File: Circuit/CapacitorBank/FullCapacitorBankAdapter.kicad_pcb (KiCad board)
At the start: 2 copper layers, 116.8 x 61 mm, 46 parts, among them J1 AC Power In, J2 Output+, J3 Output-, J4 To Control, T1 6:6:50+50, U1 L7812, U2 LM393, U3 LM393, U4 PC817

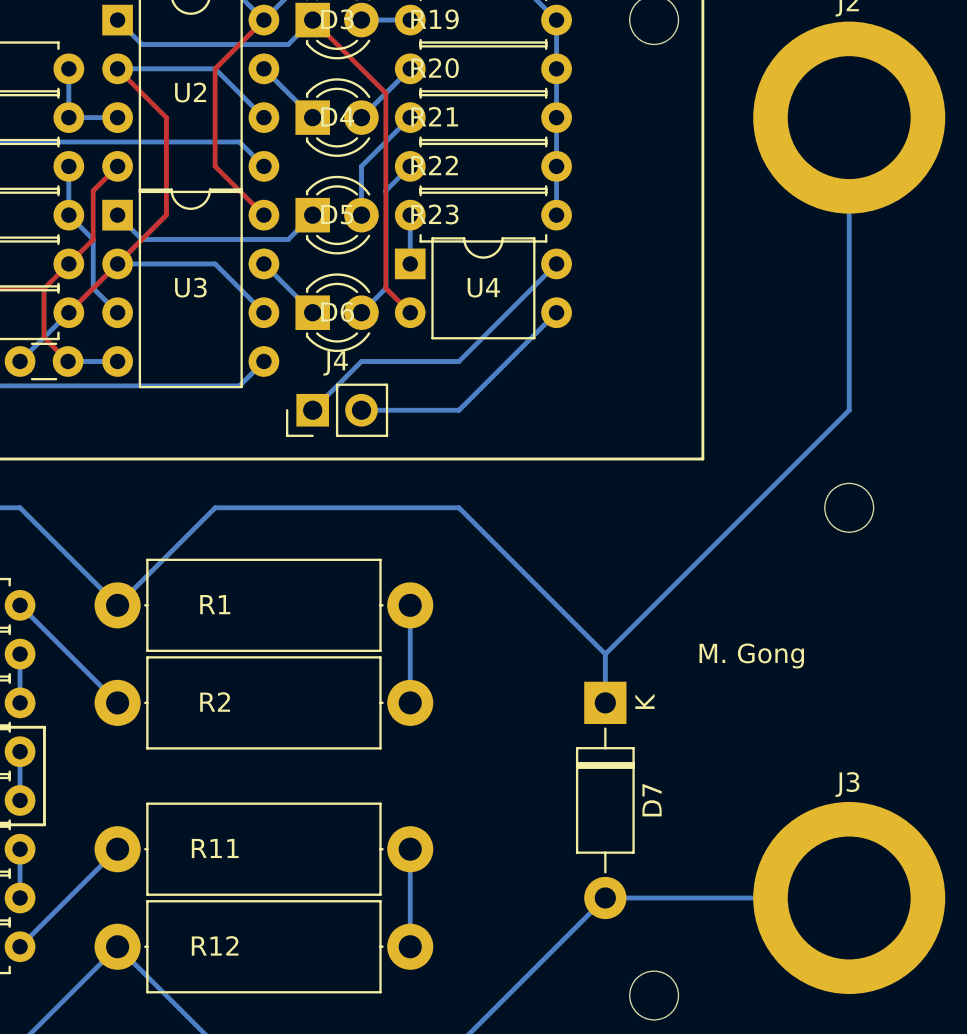
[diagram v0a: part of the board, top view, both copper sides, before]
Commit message: [Circuit][Doc] Correct the voltage calculation in full capacitor bank adapter
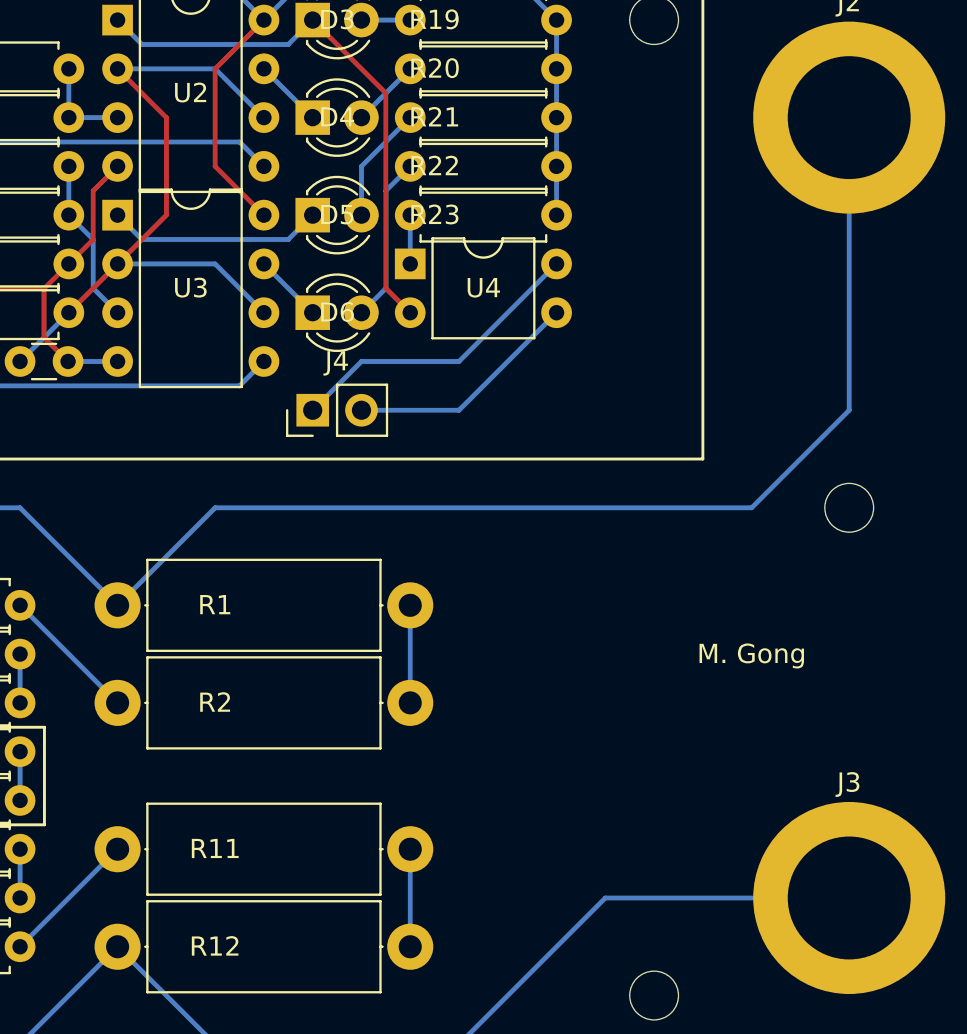
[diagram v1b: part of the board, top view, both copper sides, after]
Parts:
- removed D7: 1N4007, Diode_THT:D_DO-41_SOD81_P10.16mm_Horizontal
- T1: value 6:6:50+50 -> 6:6:33+33
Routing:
- net /PowerOut+: track 110.4 -> 101.5 mm
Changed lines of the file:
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@@
     (thickness 1.6)
     (drawings 17)
-    (tracks 161)
+    (tracks 159)
     (zones 0)
-    (modules 46)
+    (modules 45)
     (nets 40)
   )
@@
     )
   )
-  (module Diode_THT:D_DO-41_SOD81_P10.16mm_Horizontal (layer F.Cu)
-    (at 144.78 71.12 270)
-    (descr "Diode, DO-41_SOD81 series, Axial, Horizontal, pin pitch=10.16mm, , length*diameter=5.2*2.7mm^2, , http://www.diodes.com/_files/packages/DO-41%20(Plastic).pdf")
-    (tags "Diode DO-41_SOD81 series Axial Horizontal pin pitch 10.16mm  length 5.2mm diameter 2.7mm")
-    (fp_text reference D7 (at 5.08 -2.47 90) (layer F.SilkS)
-      (effects (font (size 1 1) (thickness 0.15)))
-    )
-    (fp_text value 1N4007 (at 5.08 2.47 90) (layer F.Fab)
-      (effects (font (size 1 1) (thickness 0.15)))
-    )
-    (fp_text user K (at 0 -2.1 90) (layer F.SilkS)
-      (effects (font (size 1 1) (thickness 0.15)))
-    )
-    (fp_text user K (at 0 -2.1 90) (layer F.Fab)
-      (effects (font (size 1 1) (thickness 0.15)))
-    )
-    (fp_text user %R (at 5.47 0 90) (layer F.Fab)
-      (effects (font (size 1 1) (thickness 0.15)))
-    )
-    (fp_line (start 11.51 -1.6) (end -1.35 -1.6) (layer F.CrtYd) (width 0.05))
-    (fp_line (start 11.51 1.6) (end 11.51 -1.6) (layer F.CrtYd) (width 0.05))
-    (fp_line (start -1.35 1.6) (end 11.51 1.6) (layer F.CrtYd) (width 0.05))
-    (fp_line (start -1.35 -1.6) (end -1.35 1.6) (layer F.CrtYd) (width 0.05))
-    (fp_line (start 3.14 -1.47) (end 3.14 1.47) (layer F.SilkS) (width 0.12))
-    (fp_line (start 3.38 -1.47) (end 3.38 1.47) (layer F.SilkS) (width 0.12))
-    (fp_line (start 3.26 -1.47) (end 3.26 1.47) (layer F.SilkS) (width 0.12))
-    (fp_line (start 8.82 0) (end 7.8 0) (layer F.SilkS) (width 0.12))
-    (fp_line (start 1.34 0) (end 2.36 0) (layer F.SilkS) (width 0.12))
-    (fp_line (start 7.8 -1.47) (end 2.36 -1.47) (layer F.SilkS) (width 0.12))
-    (fp_line (start 7.8 1.47) (end 7.8 -1.47) (layer F.SilkS) (width 0.12))
-    (fp_line (start 2.36 1.47) (end 7.8 1.47) (layer F.SilkS) (width 0.12))
-    (fp_line (start 2.36 -1.47) (end 2.36 1.47) (layer F.SilkS) (width 0.12))
-    (fp_line (start 3.16 -1.35) (end 3.16 1.35) (layer F.Fab) (width 0.1))
-    (fp_line (start 3.36 -1.35) (end 3.36 1.35) (layer F.Fab) (width 0.1))
-    (fp_line (start 3.26 -1.35) (end 3.26 1.35) (layer F.Fab) (width 0.1))
-    (fp_line (start 10.16 0) (end 7.68 0) (layer F.Fab) (width 0.1))
-    (fp_line (start 0 0) (end 2.48 0) (layer F.Fab) (width 0.1))
-    (fp_line (start 7.68 -1.35) (end 2.48 -1.35) (layer F.Fab) (width 0.1))
-    (fp_line (start 7.68 1.35) (end 7.68 -1.35) (layer F.Fab) (width 0.1))
-    (fp_line (start 2.48 1.35) (end 7.68 1.35) (layer F.Fab) (width 0.1))
-    (fp_line (start 2.48 -1.35) (end 2.48 1.35) (layer F.Fab) (width 0.1))
-    (pad 2 thru_hole oval (at 10.16 0 270) (size 2.2 2.2) (drill 1.1) (layers *.Cu *.Mask)
-      (net 2 /PowerOut-))
-    (pad 1 thru_hole rect (at 0 0 270) (size 2.2 2.2) (drill 1.1) (layers *.Cu *.Mask)
-      (net 1 /PowerOut+))
-    (model ${KISYS3DMOD}/Diode_THT.3dshapes/D_DO-41_SOD81_P10.16mm_Horizontal.wrl
-      (at (xyz 0 0 0))
-      (scale (xyz 1 1 1))
-      (rotate (xyz 0 0 0))
-    )
-  )
   (module Power:Heatsink_TO220_15x10mm (layer F.Cu)
     (at 78.74 34.29)
@@
       (effects (font (size 1 1) (thickness 0.15)))
     )
-    (fp_text value 6:6:50+50 (at 13 -20) (layer F.Fab)
+    (fp_text value 6:6:33+33 (at 13 -20) (layer F.Fab)
       (effects (font (size 1 1) (thickness 0.15)))
     )
@@
   (segment (start 104.14 60.96) (end 114.3 60.96) (width 0.25) (layer B.Cu) (net 1))
   (segment (start 93.98 71.12) (end 104.14 60.96) (width 0.25) (layer B.Cu) (net 1) (status 10))
-  (segment (start 124.46 60.96) (end 119.38 66.04) (width 0.25) (layer B.Cu) (net 1) (status 20))
-  (segment (start 137.16 60.96) (end 124.46 60.96) (width 0.25) (layer B.Cu) (net 1))
-  (segment (start 144.78 68.58) (end 137.16 60.96) (width 0.25) (layer B.Cu) (net 1))
-  (segment (start 144.78 71.12) (end 144.78 68.58) (width 0.25) (layer B.Cu) (net 1) (status 10))
-  (segment (start 144.78 68.58) (end 157.48 55.88) (width 0.25) (layer B.Cu) (net 1))
-  (segment (start 157.48 40.64) (end 157.48 55.88) (width 0.25) (layer B.Cu) (net 1) (status 10))
+  (segment (start 157.48 55.88) (end 157.48 40.64) (width 0.25) (layer B.Cu) (net 1))
+  (segment (start 152.4 60.96) (end 157.48 55.88) (width 0.25) (layer B.Cu) (net 1))
+  (segment (start 124.46 60.96) (end 152.4 60.96) (width 0.25) (layer B.Cu) (net 1))
+  (segment (start 119.38 66.04) (end 124.46 60.96) (width 0.25) (layer B.Cu) (net 1))
   (segment (start 88.98 76.12) (end 88.82 76.12) (width 0.25) (layer B.Cu) (net 2) (status 30))
   (segment (start 88.98 76.12) (end 88.98 81.28) (width 0.25) (layer B.Cu) (net 2) (status 30))

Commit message: [Circuit] Remove the back-to-back capacitors from capacitor bank (again)
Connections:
- net /ACPowerIn+ renamed /PowerIn+
- net /ACPowerIn- renamed /PowerIn-

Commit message: [Circuit] Upgrade to KiCad 6 format
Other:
- net class Default removed
